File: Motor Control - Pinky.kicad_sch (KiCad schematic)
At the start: 0 parts

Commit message: Update Schematic
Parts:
- added C60: 4.7uF 16V 0402, Duc_Library:C0402, symbol Duc-Capacitors:CAP CER 0402
- added C61: 100nF 16V 0603, Duc_Library:C0402, symbol Duc-Capacitors:CAP CER 0402
- added C62: 100nF 16V 0402, Duc_Library:C0402, symbol Duc-Capacitors:CAP CER 0402
- added C63: 470nF 16V 0402, Duc_Library:C0402, symbol Duc-Capacitors:CAP CER 0402
- added J5: BM09B-SRSS-TB, Duc:CONN-SMD_9P-P1.00_BM09B-SRSS-TB, symbol Duc-Connectors:BM09B-SRSS-TB
- added R16: 1R 0.1% 0402, Duc_Library:R0402, symbol Duc-Resistors:RES SMD 0402
- added R17: 10K 0.1% 0402, Duc_Library:R0402, symbol Duc-Resistors:RES SMD 0402
- added R18: 510R 0.1% 0402, Duc_Library:R0402, symbol Duc-Resistors:RES SMD 0402
- added U13: TB9051FTG,EL, Duc_Library:UQFN-28_L6.0-W6.0-P0.65-BL-EP4.0, symbol Duc-ICs:TB9051FTG,EL
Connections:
- new net: R17.1, R18.1
- new net +3.3V: J5.3, J5.8
- new net +5V: C60.2, J5.10, J5.11, R16.1
- new net +VBAT: C62.2, U13.11 (VBAT), U13.12 (VBAT), U13.24 (VBAT), U13.25 (VBAT)
- new net DGND: C60.1, C61.1, C63.1, R18.2, U13.1 (OCC), U13.27 (TEST1), U13.28 (TEST2), U13.3 (ENB), U13.4 (AGND)
- new net DIAG_M: U13.18 (DIAG)
- new net ECA_M: J5.6
- new net ECB_M: J5.7
- new net ECC_M: J5.2
- new net EN_M: U13.5 (EN)
- new net GND: C62.1, J5.1, J5.5, U13.15 (PGND), U13.16 (PGND), U13.17 (PGND), U13.19 (PGND), U13.20 (PGND), U13.21 (PGND), U13.29 (EP)
- new net OUT1_M: J5.4, U13.13 (OUT1), U13.14 (OUT1)
- new net OUT2_M: J5.9, U13.22 (OUT2), U13.23 (OUT2)
- new net PWMA_M: U13.8 (PWM1)
- new net PWMB_M: U13.9 (PWM2)
- new net VCC_M: C61.2, R16.2, U13.2 (VCC)
- new net _OCM_M: C63.2, R17.2, U13.7 (OCM)
- no-connect marks 0 -> 3

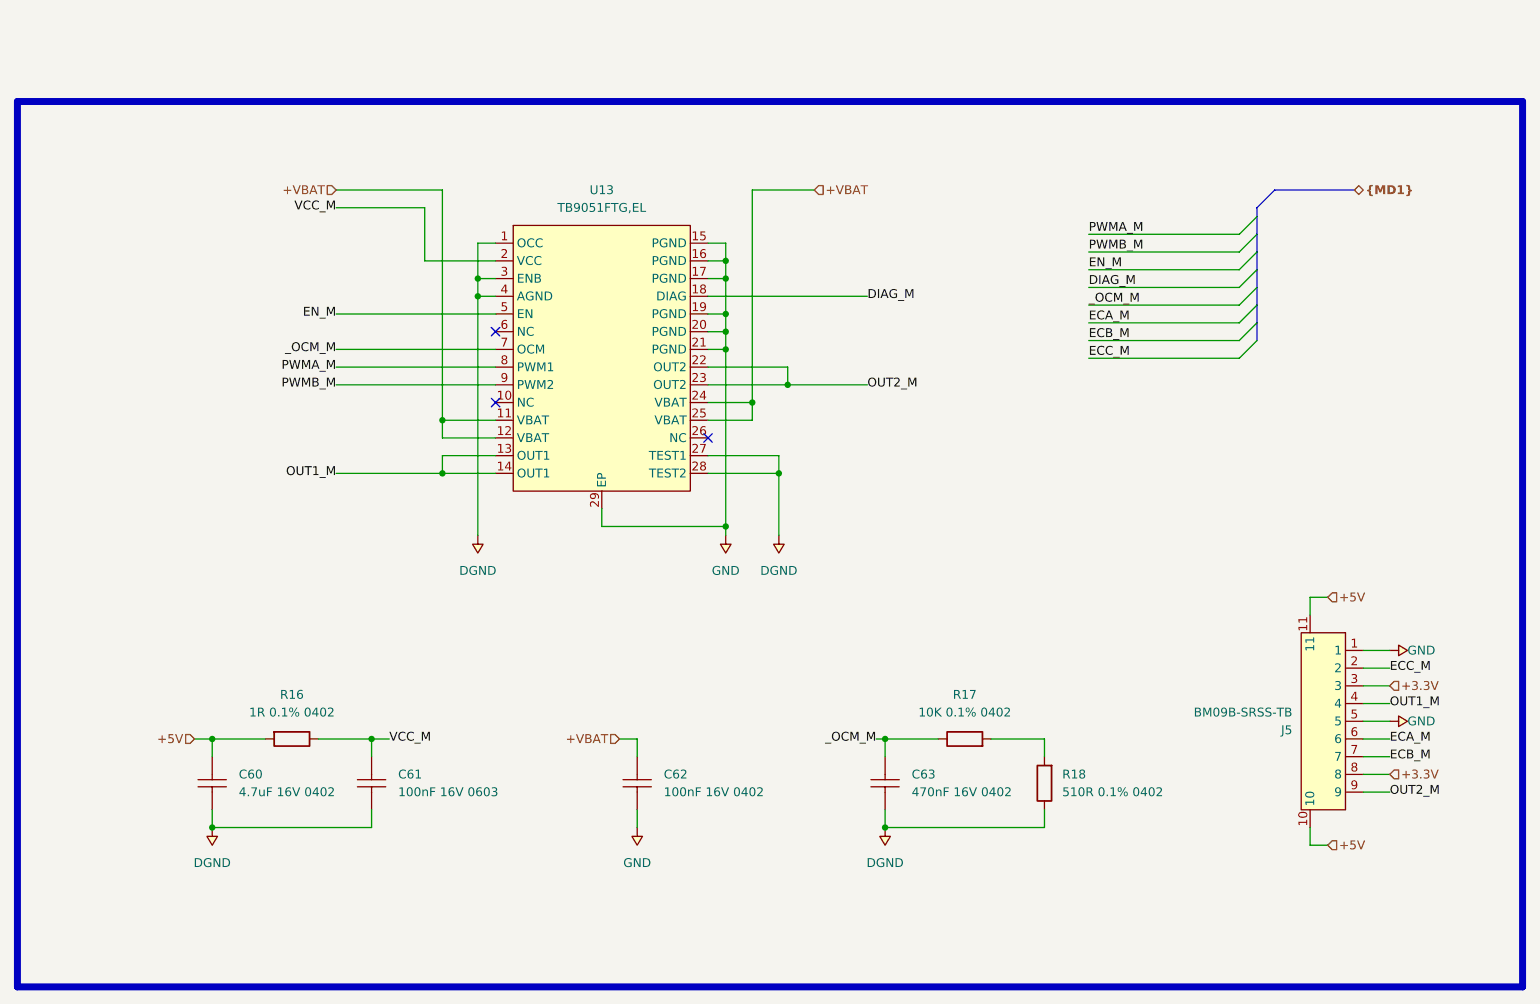
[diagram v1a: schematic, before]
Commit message: Update Motor Schematic
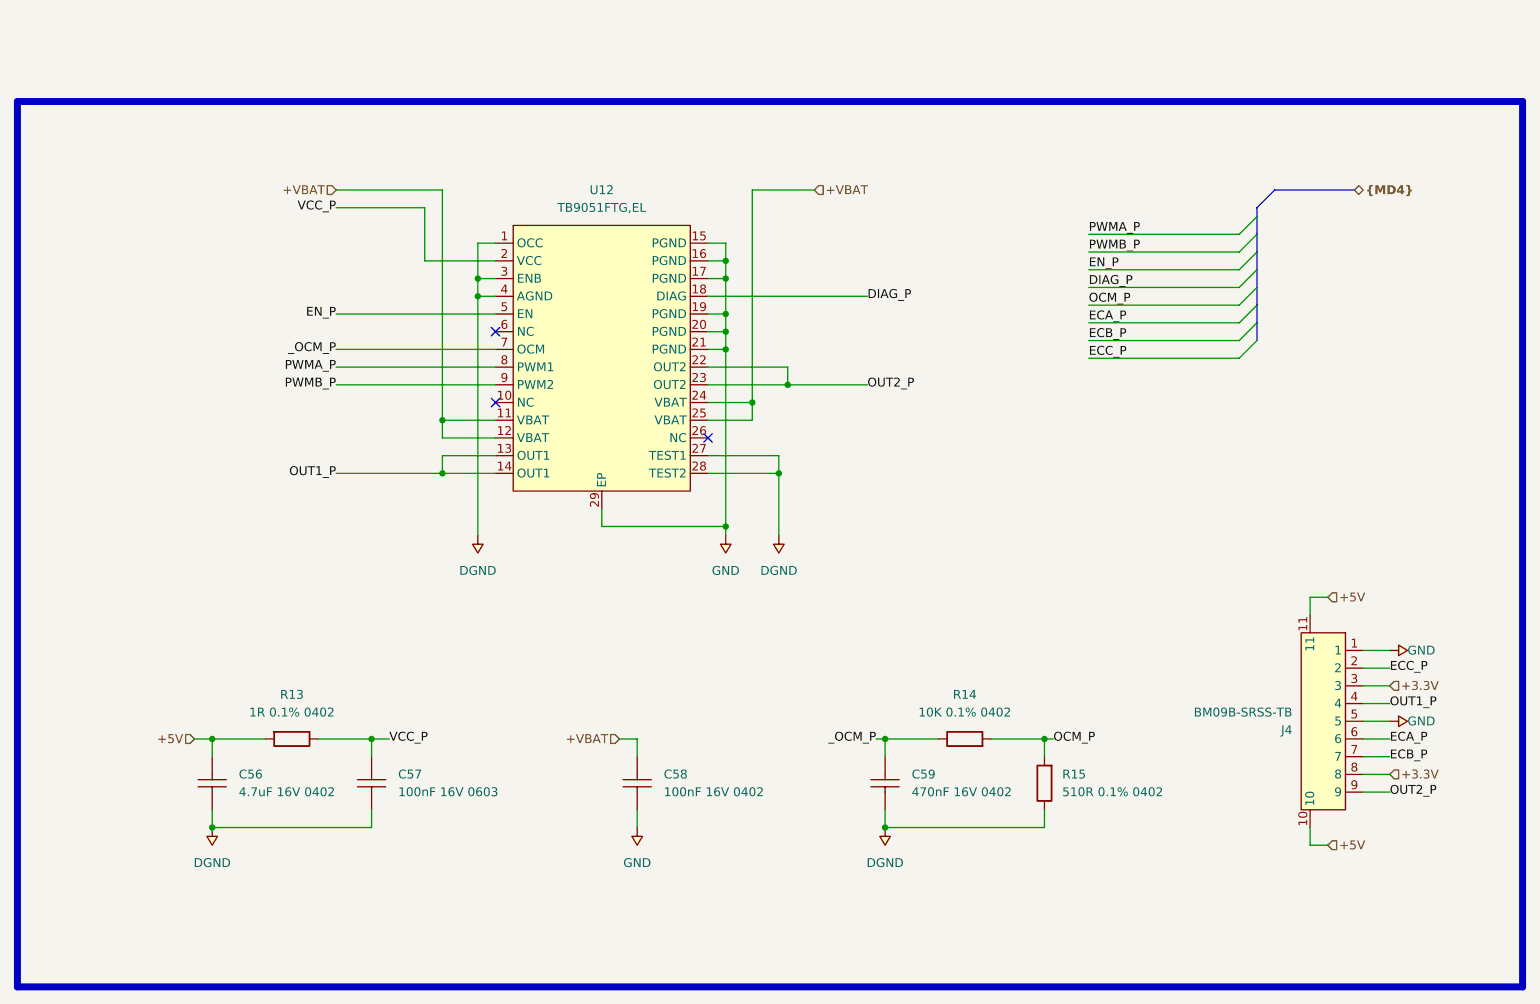
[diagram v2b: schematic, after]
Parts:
- removed C60: 4.7uF 16V 0402, Duc_Library:C0402, symbol Duc-Capacitors:CAP CER 0402
- removed C61: 100nF 16V 0603, Duc_Library:C0402, symbol Duc-Capacitors:CAP CER 0402
- removed C62: 100nF 16V 0402, Duc_Library:C0402, symbol Duc-Capacitors:CAP CER 0402
- removed C63: 470nF 16V 0402, Duc_Library:C0402, symbol Duc-Capacitors:CAP CER 0402
- removed J5: BM09B-SRSS-TB, Duc:CONN-SMD_9P-P1.00_BM09B-SRSS-TB, symbol Duc-Connectors:BM09B-SRSS-TB
- removed R16: 1R 0.1% 0402, Duc_Library:R0402, symbol Duc-Resistors:RES SMD 0402
- removed R17: 10K 0.1% 0402, Duc_Library:R0402, symbol Duc-Resistors:RES SMD 0402
- removed R18: 510R 0.1% 0402, Duc_Library:R0402, symbol Duc-Resistors:RES SMD 0402
- removed U13: TB9051FTG,EL, Duc_Library:UQFN-28_L6.0-W6.0-P0.65-BL-EP4.0, symbol Duc-ICs:TB9051FTG,EL
- added C56: 4.7uF 16V 0402, Duc_Library:C0402, symbol Duc-Capacitors:CAP CER 0402
- added C57: 100nF 16V 0603, Duc_Library:C0402, symbol Duc-Capacitors:CAP CER 0402
- added C58: 100nF 16V 0402, Duc_Library:C0402, symbol Duc-Capacitors:CAP CER 0402
- added C59: 470nF 16V 0402, Duc_Library:C0402, symbol Duc-Capacitors:CAP CER 0402
- added J4: BM09B-SRSS-TB, Duc:CONN-SMD_9P-P1.00_BM09B-SRSS-TB, symbol Duc-Connectors:BM09B-SRSS-TB
- added R13: 1R 0.1% 0402, Duc_Library:R0402, symbol Duc-Resistors:RES SMD 0402
- added R14: 10K 0.1% 0402, Duc_Library:R0402, symbol Duc-Resistors:RES SMD 0402
- added R15: 510R 0.1% 0402, Duc_Library:R0402, symbol Duc-Resistors:RES SMD 0402
- added U12: TB9051FTG,EL, Duc_Library:UQFN-28_L6.0-W6.0-P0.65-BL-EP4.0, symbol Duc-ICs:TB9051FTG,EL
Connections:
- net +3.3V: now also J4.3, J4.8
- net +5V: now also C56.2, J4.10, J4.11, R13.1
- net +VBAT: now also C58.2, U12.11 (VBAT), U12.12 (VBAT), U12.24 (VBAT), U12.25 (VBAT)
- net DGND: now also C56.1, C57.1, C59.1, R15.2, U12.1 (OCC), U12.27 (TEST1), U12.28 (TEST2), U12.3 (ENB), U12.4 (AGND)
- net GND: now also C58.1, J4.1, J4.5, U12.15 (PGND), U12.16 (PGND), U12.17 (PGND), U12.19 (PGND), U12.20 (PGND), U12.21 (PGND), U12.29 (EP)
- new net DIAG_P: U12.18 (DIAG)
- new net ECA_P: J4.6
- new net ECB_P: J4.7
- new net ECC_P: J4.2
- new net EN_P: U12.5 (EN)
- new net OCM_P: R14.1, R15.1
- new net OUT1_P: J4.4, U12.13 (OUT1), U12.14 (OUT1)
- new net OUT2_P: J4.9, U12.22 (OUT2), U12.23 (OUT2)
- new net PWMA_P: U12.8 (PWM1)
- new net PWMB_P: U12.9 (PWM2)
- new net VCC_P: C57.2, R13.2, U12.2 (VCC)
- new net _OCM_P: C59.2, R14.2, U12.7 (OCM)

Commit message: Update Schematic
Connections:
- net DGND is gone; now on net GND: C56.1, C57.1, C59.1, R15.2, U12.1 (OCC), U12.27 (TEST1), U12.28 (TEST2), U12.3 (ENB), U12.4 (AGND)
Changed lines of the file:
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@@
 		)
 	)
-	(junction
-		(at 147.32 78.74)
-		(diameter 0)
-		(color 0 0 0 0)
+	(text_box "[${#}] ${SHEETNAME}"
+		(exclude_from_sim no)
+		(at 12.7 12.7 0)
+		(size 271.78 12.7)
+		(margins 4.4999 4.4999 4.4999 4.4999)
+		(stroke
+			(width -0.0001)
+			(type solid)
+		)
+		(fill
+			(type none)
+		)
+		(effects
+			(font
+				(face "Times New Roman")
+				(size 6 6)
+				(thickness 1.2)
+				(bold yes)
+				(color 162 22 34 1)
+			)
+		)
 	)
 	(junction
@@
 	)
 	(junction
+		(at 139.7 78.74)
+		(diameter 0)
+		(color 0 0 0 0)
+	)
+	(junction
 		(at 185.42 116.84)
 		(diameter 0)
@@
 	)
 	(junction
-		(at 162.56 129.54)
+		(at 139.7 58.42)
 		(diameter 0)
 		(color 0 0 0 0)
 	)
 	(junction
-		(at 139.7 58.42)
+		(at 139.7 76.2)
 		(diameter 0)
 		(color 0 0 0 0)
@@
 	)
 	(junction
+		(at 66.04 129.54)
+		(diameter 0)
+		(color 0 0 0 0)
+	)
+	(junction
 		(at 104.14 50.8)
 		(diameter 0)
@@
 	)
 	(junction
+		(at 121.92 86.36)
+		(diameter 0)
+		(color 0 0 0 0)
+	)
+	(junction
+		(at 162.56 129.54)
+		(diameter 0)
+		(color 0 0 0 0)
+	)
+	(junction
 		(at 139.7 55.88)
 		(diameter 0)
@@
 	)
 	(junction
-		(at 66.04 129.54)
-		(diameter 0)
-		(color 0 0 0 0)
-	)
-	(junction
 		(at 99.06 71.12)
 		(diameter 0)
@@
 	(wire
 		(pts
-			(xy 137.16 76.2) (xy 147.32 76.2)
+			(xy 137.16 76.2) (xy 139.7 76.2)
 		)
 		(stroke
@@
 	(wire
 		(pts
+			(xy 104.14 86.36) (xy 121.92 86.36)
+		)
+		(stroke
+			(width 0)
+			(type default)
+		)
+	)
+	(wire
+		(pts
 			(xy 191.77 57.15) (xy 213.36 57.15)
 		)
@@
 	(wire
 		(pts
+			(xy 139.7 76.2) (xy 139.7 78.74)
+		)
+		(stroke
+			(width 0)
+			(type default)
+		)
+	)
+	(wire
+		(pts
 			(xy 148.59 63.5) (xy 148.59 66.04)
 		)
@@
 	(wire
 		(pts
-			(xy 104.14 53.34) (xy 104.14 87.63)
+			(xy 104.14 53.34) (xy 104.14 86.36)
 		)
 		(stroke
@@
 	(wire
 		(pts
-			(xy 147.32 78.74) (xy 147.32 87.63)
-		)
-		(stroke
-			(width 0)
-			(type default)
-		)
-	)
-	(wire
-		(pts
 			(xy 231.14 116.84) (xy 234.95 116.84)
 		)
@@
 	(wire
 		(pts
+			(xy 139.7 78.74) (xy 139.7 86.36)
+		)
+		(stroke
+			(width 0)
+			(type default)
+		)
+	)
+	(wire
+		(pts
 			(xy 191.77 52.07) (xy 213.36 52.07)
 		)
@@
 	(wire
 		(pts
-			(xy 147.32 76.2) (xy 147.32 78.74)
-		)
-		(stroke
-			(width 0)
-			(type default)
-		)
-	)
-	(wire
-		(pts
 			(xy 99.06 76.2) (xy 106.68 76.2)
 		)
@@
 	(wire
 		(pts
-			(xy 137.16 78.74) (xy 147.32 78.74)
+			(xy 137.16 78.74) (xy 139.7 78.74)
 		)
 		(stroke
@@
 	(wire
 		(pts
-			(xy 139.7 60.96) (xy 139.7 86.36)
+			(xy 139.7 60.96) (xy 139.7 76.2)
 		)
 		(stroke
@@
 	)
 	(symbol
-		(lib_id "Power_symbols:DGND")
-		(at 147.32 86.36 180)
-		(unit 1)
-		(exclude_from_sim no)
-		(in_bom no)
-		(on_board no)
-		(dnp no)
-		(fields_autoplaced yes)
-		(property "Reference" "#PWR050"
-			(at 147.32 86.36 0)
-			(effects
-				(font
-					(size 1.27 1.27)
-				)
-				(hide yes)
-			)
-		)
-		(property "Value" "DGND"
-			(at 147.32 92.71 0)
-			(effects
-				(font
-					(size 1.27 1.27)
-				)
-			)
-		)
-		(property "Footprint" ""
-			(at 147.32 86.36 0)
-			(effects
-				(font
-					(size 1.27 1.27)
-				)
-				(hide yes)
-			)
-		)
-		(property "Datasheet" ""
-			(at 147.32 86.36 0)
-			(effects
-				(font
-					(size 1.27 1.27)
-				)
-				(hide yes)
-			)
-		)
-		(property "Description" "Power Symbol - Digital Ground"
-			(at 147.32 86.36 0)
-			(effects
-				(font
-					(size 1.27 1.27)
-				)
-				(hide yes)
-			)
-		)
-		(pin "1"
-		)
-		(instances
-			(project "Master_Hand_Kicad"
-				(path "/f9e05184-c88b-4a88-ae9c-ab2bdb32be7c/c5103ceb-5325-4a84-a025-9638a412984e/0ad8e17f-d145-48f3-a9e5-8d5e790e9ed0"
-					(reference "#PWR050")
-					(unit 1)
-				)
-			)
-		)
-	)
-	(symbol
 		(lib_id "Power_symbols:GND")
 		(at 233.68 114.3 270)
@@
 	)
 	(symbol
-		(lib_id "Power_symbols:DGND")
+		(lib_id "Power_symbols:GND")
 		(at 162.56 128.27 180)
 		(unit 1)
@@
 		(property "Reference" "#PWR051"
 			(at 162.56 128.27 0)
-			(effects
-				(font
-					(size 1.27 1.27)
-				)
-				(hide yes)
-			)
-		)
-		(property "Value" "DGND"
+			(do_not_autoplace yes)
+			(effects
+				(font
+					(size 1.27 1.27)
+				)
+				(hide yes)
+			)
+		)
+		(property "Value" "GND"
 			(at 162.56 134.62 0)
 			(effects
@@
 			)
 		)
-		(property "Description" "Power Symbol - Digital Ground"
+		(property "Description" "Power Symbol - Global Ground"
 			(at 162.56 128.27 0)
 			(effects
@@
 				(path "/f9e05184-c88b-4a88-ae9c-ab2bdb32be7c/c5103ceb-5325-4a84-a025-9638a412984e/0ad8e17f-d145-48f3-a9e5-8d5e790e9ed0"
 					(reference "#PWR051")
-					(unit 1)
-				)
-			)
-		)
-	)
-	(symbol
-		(lib_id "Power_symbols:DGND")
-		(at 66.04 128.27 180)
-		(unit 1)
-		(exclude_from_sim no)
-		(in_bom no)
-		(on_board no)
-		(dnp no)
-		(fields_autoplaced yes)
-		(property "Reference" "#PWR046"
-			(at 66.04 128.27 0)
-			(effects
-				(font
-					(size 1.27 1.27)
-				)
-				(hide yes)
-			)
-		)
-		(property "Value" "DGND"
-			(at 66.04 134.62 0)
-			(effects
-				(font
-					(size 1.27 1.27)
-				)
-			)
-		)
-		(property "Footprint" ""
-			(at 66.04 128.27 0)
-			(effects
-				(font
-					(size 1.27 1.27)
-				)
-				(hide yes)
-			)
-		)
-		(property "Datasheet" ""
-			(at 66.04 128.27 0)
-			(effects
-				(font
-					(size 1.27 1.27)
-				)
-				(hide yes)
-			)
-		)
-		(property "Description" "Power Symbol - Digital Ground"
-			(at 66.04 128.27 0)
-			(effects
-				(font
-					(size 1.27 1.27)
-				)
-				(hide yes)
-			)
-		)
-		(pin "1"
-		)
-		(instances
-			(project "Master_Hand_Kicad"
-				(path "/f9e05184-c88b-4a88-ae9c-ab2bdb32be7c/c5103ceb-5325-4a84-a025-9638a412984e/0ad8e17f-d145-48f3-a9e5-8d5e790e9ed0"
-					(reference "#PWR046")
 					(unit 1)
 				)
@@
 	)
 	(symbol
-		(lib_id "Power_symbols:DGND")
-		(at 104.14 86.36 180)
+		(lib_id "Power_symbols:GND")
+		(at 66.04 128.27 180)
 		(unit 1)
 		(exclude_from_sim no)
@@
 		(dnp no)
 		(fields_autoplaced yes)
-		(property "Reference" "#PWR047"
-			(at 104.14 86.36 0)
-			(effects
-				(font
-					(size 1.27 1.27)
-				)
-				(hide yes)
-			)
-		)
-		(property "Value" "DGND"
-			(at 104.14 92.71 0)
+		(property "Reference" "#PWR050"
+			(at 66.04 128.27 0)
+			(do_not_autoplace yes)
+			(effects
+				(font
+					(size 1.27 1.27)
+				)
+				(hide yes)
+			)
+		)
+		(property "Value" "GND"
+			(at 66.04 134.62 0)
 			(effects
 				(font
@@
 		)
 		(property "Footprint" ""
-			(at 104.14 86.36 0)
+			(at 66.04 128.27 0)
 			(effects
 				(font
@@
 		)
 		(property "Datasheet" ""
-			(at 104.14 86.36 0)
-			(effects
-				(font
-					(size 1.27 1.27)
-				)
-				(hide yes)
-			)
-		)
-		(property "Description" "Power Symbol - Digital Ground"
-			(at 104.14 86.36 0)
+			(at 66.04 128.27 0)
+			(effects
+				(font
+					(size 1.27 1.27)
+				)
+				(hide yes)
+			)
+		)
+		(property "Description" "Power Symbol - Global Ground"
+			(at 66.04 128.27 0)
 			(effects
 				(font
@@
 			(project "Master_Hand_Kicad"
 				(path "/f9e05184-c88b-4a88-ae9c-ab2bdb32be7c/c5103ceb-5325-4a84-a025-9638a412984e/0ad8e17f-d145-48f3-a9e5-8d5e790e9ed0"
-					(reference "#PWR047")
+					(reference "#PWR050")
 					(unit 1)
 				)

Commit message: Update Schematic
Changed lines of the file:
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@@
+		)
+	)
+	(rectangle
+		(start 177.8 25.4)
+		(end 254 76.2)
+		(stroke
+			(width 1)
+			(type default)
+			(color 200 0 0 1)
+		)
+		(fill
+			(type none)
 		)
 	)

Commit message: Update Schematic
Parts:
- removed J4: BM09B-SRSS-TB, Duc:CONN-SMD_9P-P1.00_BM09B-SRSS-TB, symbol Duc-Connectors:BM09B-SRSS-TB
- added C92, C93: 100nF 16V 0402, Duc_Library:C0402, symbol Duc-Capacitors:CAP CER 0402
- added J6: BM09B-SRSS-TB, Duc:CONN-SMD_9P-P1.00_BM09B-SRSS-TB, symbol Duc-Connectors:BM09B-SRSS-TB
- added R65: 1K 0.1% 0402, Duc_Library:R0402, symbol Duc-Resistors:RES SMD 0402
- added R66, R74: 220R 0.1% 0402, Duc_Library:R0402, symbol Duc-Resistors:RES SMD 0402
- R17: renamed from R14; value 10K 0.1% 0402 -> 1K 0.1% 0402
- R18: renamed from R15; value 510R 0.1% 0402 -> 220R 0.1% 0402
- renumbered C56 to C60, C57 to C61, C58 to C62, C59 to C63, R13 to R16, U12 to U11
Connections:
- net DIAG_P: now also R66.2; no longer U11.18 (DIAG)
- net ECA_P: now also J6.6
- net ECB_P: now also J6.7
- net ECC_P: now also C93.2, R74.2
- net GND: now also C92.1, C93.1, J6.1, J6.10, J6.11, J6.5
- net OUT1_P: now also J6.4
- net OUT2_P: now also J6.9
- new net +3V3: J6.8, R65.2
- new net +A3V3: C92.2, J6.3
- new net _DIAG_P: R65.1, R66.1, U11.18 (DIAG)
- new net _ECC_P: J6.2, R74.1
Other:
- moved on the sheet: C60, C61, C62, C63, R16, R17, R18

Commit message: Update Schematic
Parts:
- renumbered C60 to C70, C61 to C71, C62 to C72, C63 to C73, C92 to C74, C93 to C75, R16 to R25, R17 to R26, R66 to R27, R18 to R28, R65 to R29, R74 to R30

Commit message: Update Schematic
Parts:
- C70: value 4.7uF 16V 0402 -> CAP CER 0402
- C71: value 100nF 16V 0603 -> CAP CER 0402
- C72, C74, C75: value 100nF 16V 0402 -> CAP CER 0402
- C73: value 470nF 16V 0402 -> CAP CER 0402
- R25: value 1R 0.1% 0402 -> RES 0402
- R26, R29: value 1K 0.1% 0402 -> RES 0402
- R27, R28, R30: value 220R 0.1% 0402 -> RES 0402

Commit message: Update Schematic
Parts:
- removed C70, C71, C72, C73, C74, C75: CAP CER 0402, Duc_Library:C0402, symbol Duc-Capacitors:CAP CER 0402
- removed R25, R26, R27, R28, R29, R30: RES 0402, Duc_Library:R0402, symbol Duc-Resistors:RES SMD 0402
- added C70: 4.7uF 50V 0603, Duc:C0603, symbol Duc-Capacitors:CAP CER 0603
- added C71, C72, C74, C75: 100nF 50V 0603, Duc:C0603, symbol Duc-Capacitors:CAP CER 0603
- added C73: 470nF 50V 0603, Duc:C0603, symbol Duc-Capacitors:CAP CER 0603
- added R25: 1R 0.1% 0603, Duc:R0603, symbol Duc-Resistors:RES SMD 0603
- added R26, R29: 1K 0.1% 0603, Duc:R0603, symbol Duc-Resistors:RES SMD 0603
- added R27, R28, R30: 220R 0.1% 0603, Duc:R0603, symbol Duc-Resistors:RES SMD 0603
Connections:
- net +3V3: now also R29.2
- net +5V: now also C70.2, R25.1
- net +A3V3: now also C74.2
- net +VBAT: now also C72.2
- net DIAG_P: now also R27.2
- net ECC_P: now also C75.2, R30.2
- net GND: now also C70.1, C71.1, C72.1, C73.1, C74.1, C75.1, R28.2
- net OCM_P: now also R26.1, R28.1
- net VCC_P: now also C71.2, R25.2
- net _DIAG_P: now also R27.1, R29.1
- net _ECC_P: now also R30.1
- net _OCM_P: now also C73.2, R26.2
